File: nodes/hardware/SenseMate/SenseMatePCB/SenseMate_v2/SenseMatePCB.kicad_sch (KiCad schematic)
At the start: 15 parts, among them J1 Conn_01x04, M1 Motor_DC, Q1 2SC1815, Q2 2SC1815, SW5 SW_DPDT_x2, U1 XIAO-nRF52840-Plus-SMD, U2 RFM95W-868S2

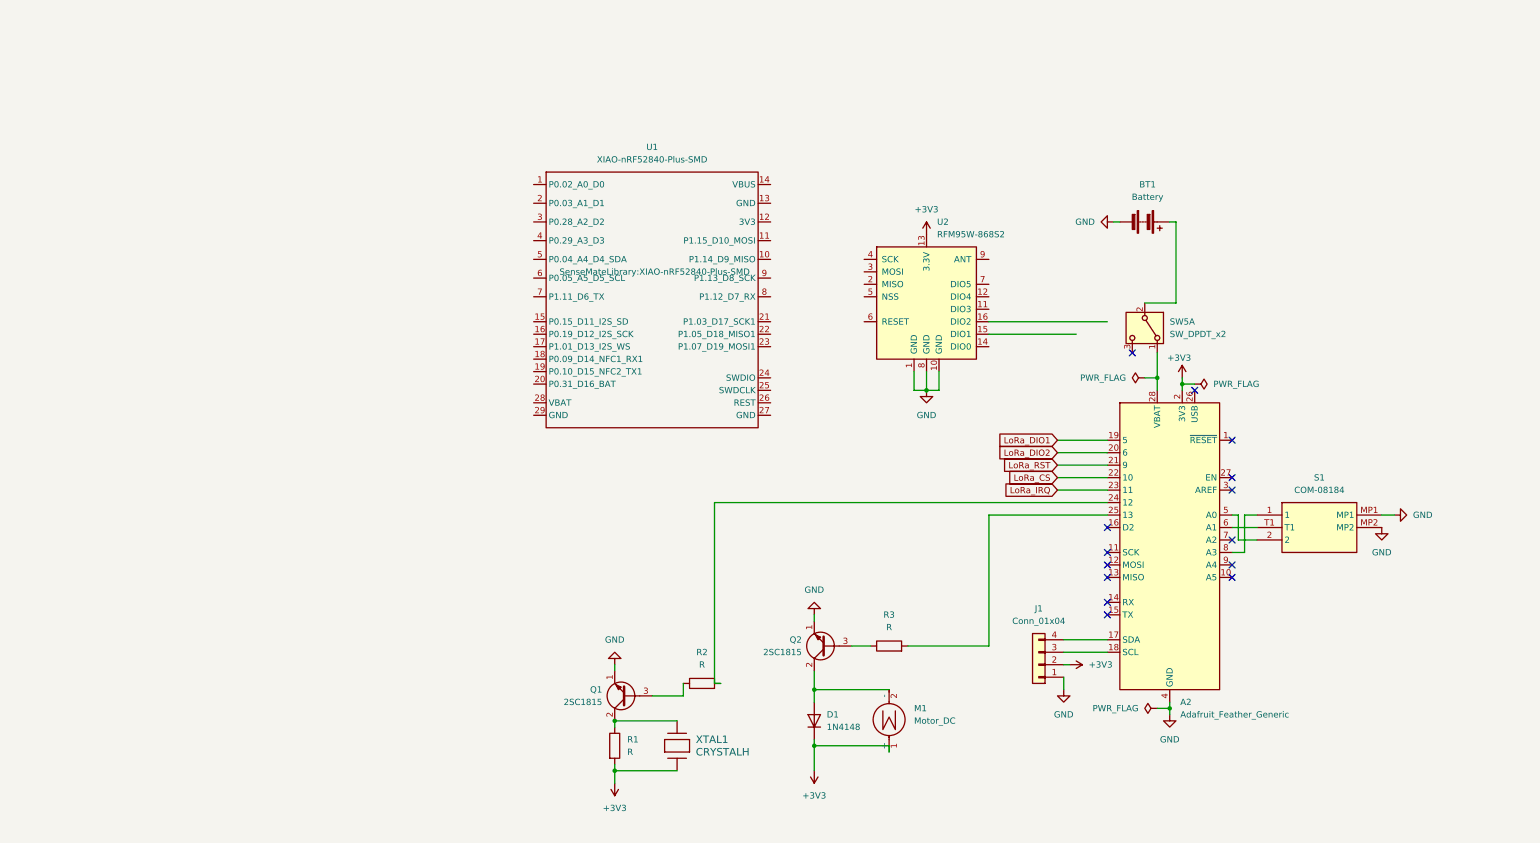
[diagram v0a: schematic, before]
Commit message: Aktualisierung der Verbindungen und Kommentare für offene Verbindungen.
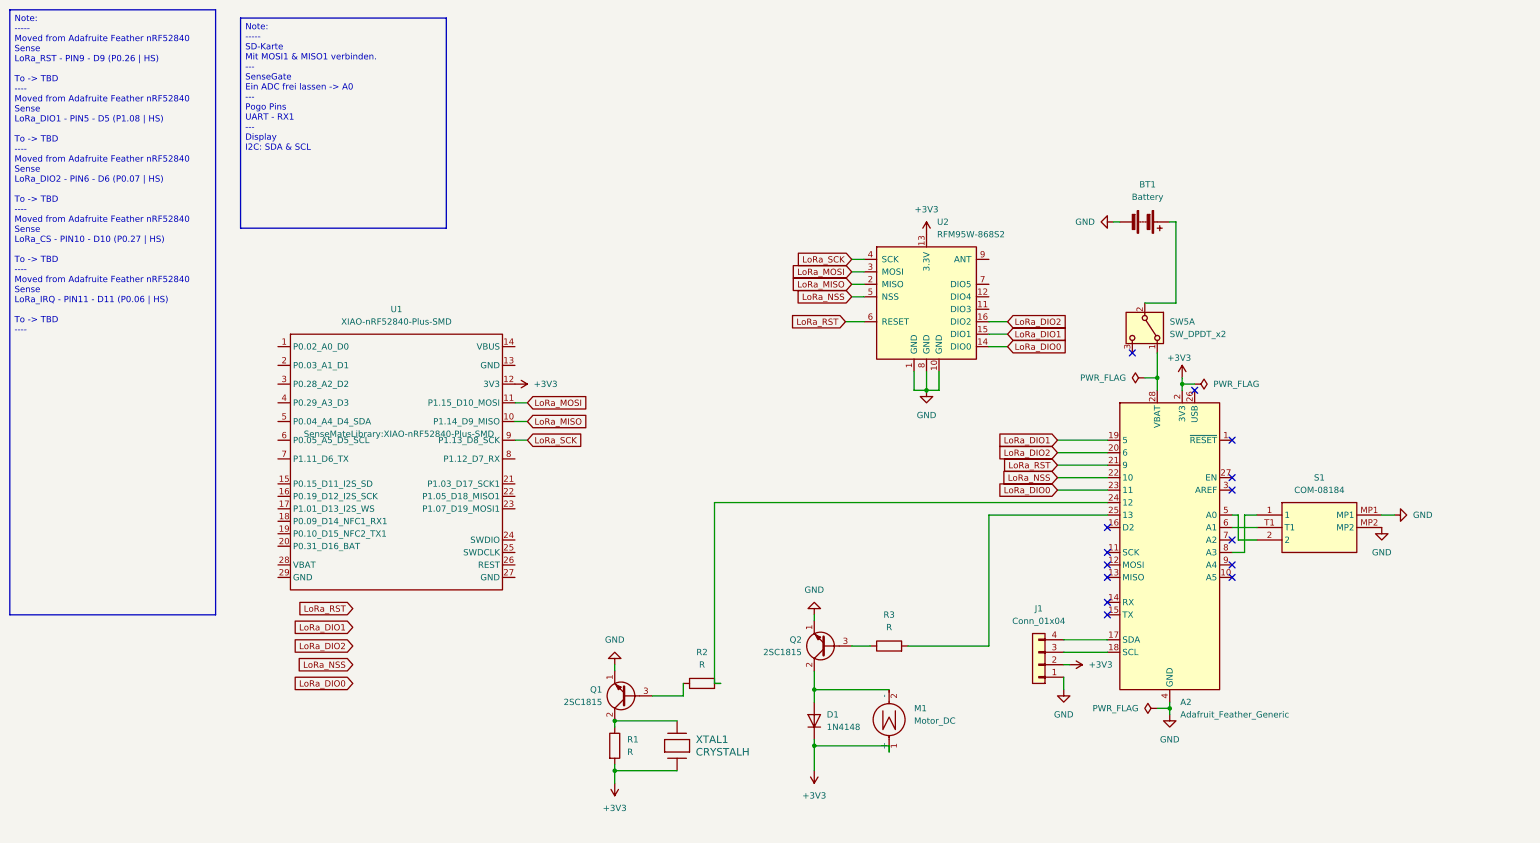
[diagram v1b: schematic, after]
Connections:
- net LoRa_CS is gone; now on net LoRa_NSS: A2.22 (10)
- net LoRa_IRQ is gone; now on net LoRa_DIO0: A2.23 (11)
- net +3V3: now also U1.12 (3V3)
- net LoRa_DIO1: now also U2.15 (DIO1)
- net LoRa_DIO2: now also U2.16 (DIO2)
- net LoRa_RST: now also U2.6 (RESET)
- net LoRa_DIO0: now reaches U2.14 (DIO0)
- net LoRa_MISO: now reaches U2.2 (MISO)
- net LoRa_MISO: now also U1.10 (P1.14_D9_MISO)
- net LoRa_MOSI: now reaches U2.3 (MOSI)
- net LoRa_MOSI: now also U1.11 (P1.15_D10_MOSI)
- net LoRa_SCK: now reaches U2.4 (SCK)
- net LoRa_SCK: now also U1.9 (P1.13_D8_SCK)
- net LoRa_NSS: now reaches U2.5 (NSS)
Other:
- moved on the sheet: U1

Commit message: 26-finished marking used pins
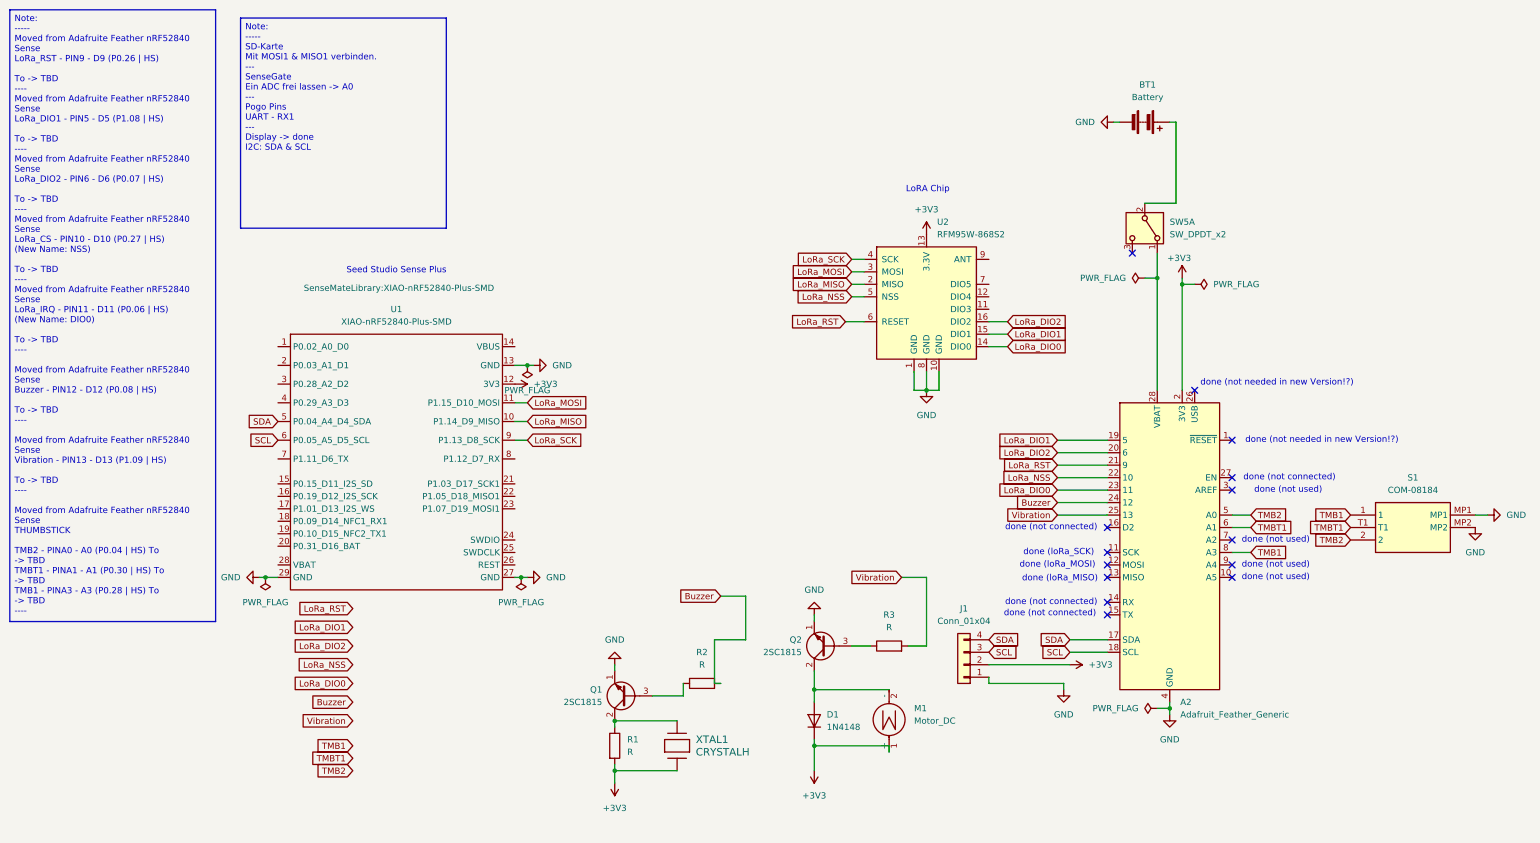
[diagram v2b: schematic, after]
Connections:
- net GND: now also U1.13 (GND), U1.27 (GND), U1.29 (GND)
- net SDA: now reaches A2.17 (SDA), J1.4 (Pin_4)
- net SDA: now also U1.5 (P0.04_A4_D4_SDA)
- net SCL: now reaches A2.18 (SCL), J1.3 (Pin_3)
- net SCL: now also U1.6 (P0.05_A5_D5_SCL)
- net Buzzer: now reaches A2.24 (12), R2.2
- net Vibration: now reaches A2.25 (13), R3.2
- net TMB2: now reaches A2.5 (A0), S1.2
- net TMBT1: now reaches A2.6 (A1), S1.T1
- net TMB1: now reaches A2.8 (A3), S1.1
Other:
- note added: "LoRA Chip"
- note added: "Seed Studio Sense Plus"
- note added: "done (loRa_MISO)"
- note added: "done (loRa_MOSI)"
- note added: "done (loRa_SCK)"
- note added: "done (not connected)"
- note added: "done (not needed in new Version!?)"
- note added: "done (not used)"
- moved on the sheet: BT1, J1, S1, SW5A

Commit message: 26-finished all connections from feather carried over
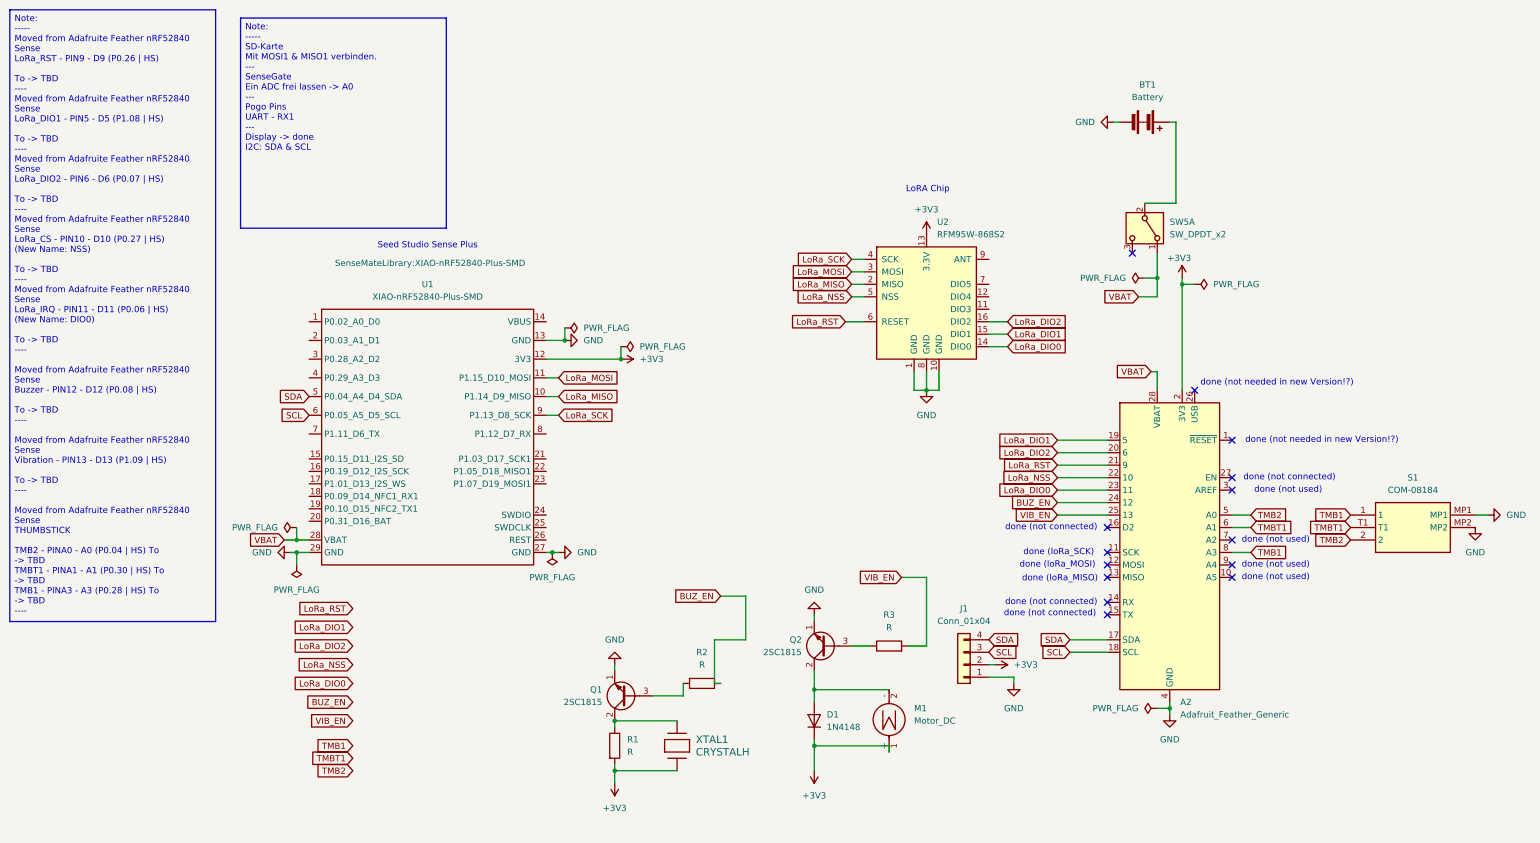
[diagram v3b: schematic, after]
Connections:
- net VBAT: now reaches A2.28 (VBAT), SW5.1 (A)
- net VBAT: now also U1.28 (VBAT)
- net Buzzer renamed BUZ_EN
- net Vibration renamed VIB_EN
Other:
- moved on the sheet: U1

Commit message: 26-Finalisierung der Verbindunen zwischen den Geräten und Aufräumen des Schemas
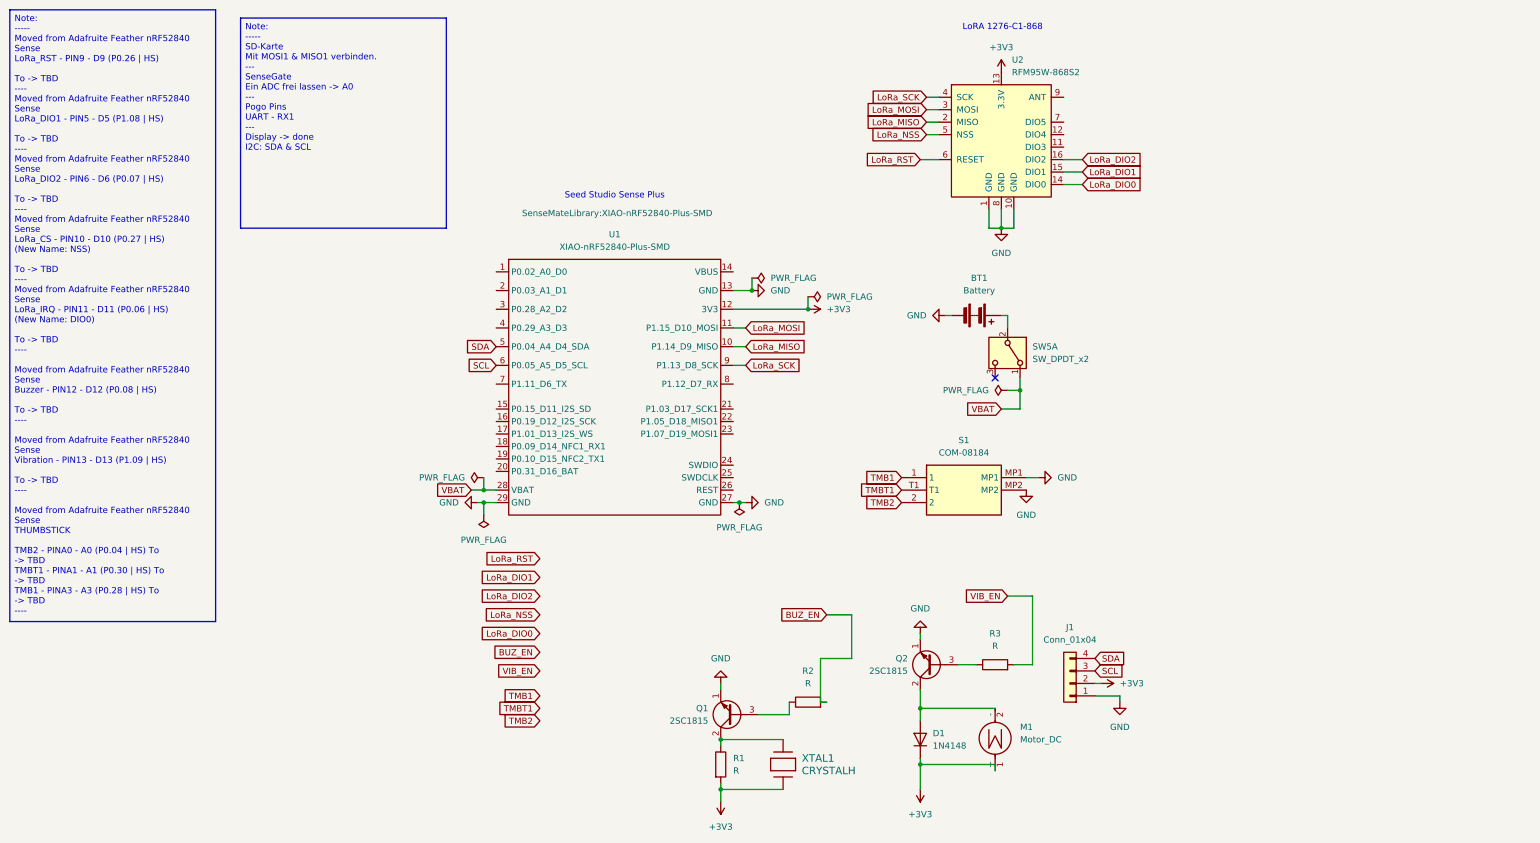
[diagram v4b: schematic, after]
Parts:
- removed A2: Adafruit_Feather_Generic, SenseMateLibrary:Adafruit_Feather_Sense, symbol SenseMateLibrary:Adafruit_Feather_Generic
- SW5: footprint SenseMate_Pwr_Button_:OS102011MA1QN1 -> SenseMateLibrary:OS102011MA1QN1
- XTAL1: footprint XTAL_PS1240P02BT_TDK -> SenseMateLibrary:PS1240P02BT
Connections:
- no-connect marks 14 -> 1
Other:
- note added: "LoRA 1276-C1-868"
- note removed: "LoRA Chip"
- note removed: "done (loRa_MISO)"
- note removed: "done (loRa_MOSI)"
- note removed: "done (loRa_SCK)"
- note removed: "done (not connected)"
- note removed: "done (not needed in new Version!?)"
- note removed: "done (not used)"
- moved on the sheet: BT1, D1, J1, M1, Q1, Q2, R1, R2, R3, S1, SW5A, U1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

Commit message: fehlende 3D symboly für SeedStudio und LoraChip hinzugefügt, Netzte Verbunden, Kommentare ergänzt
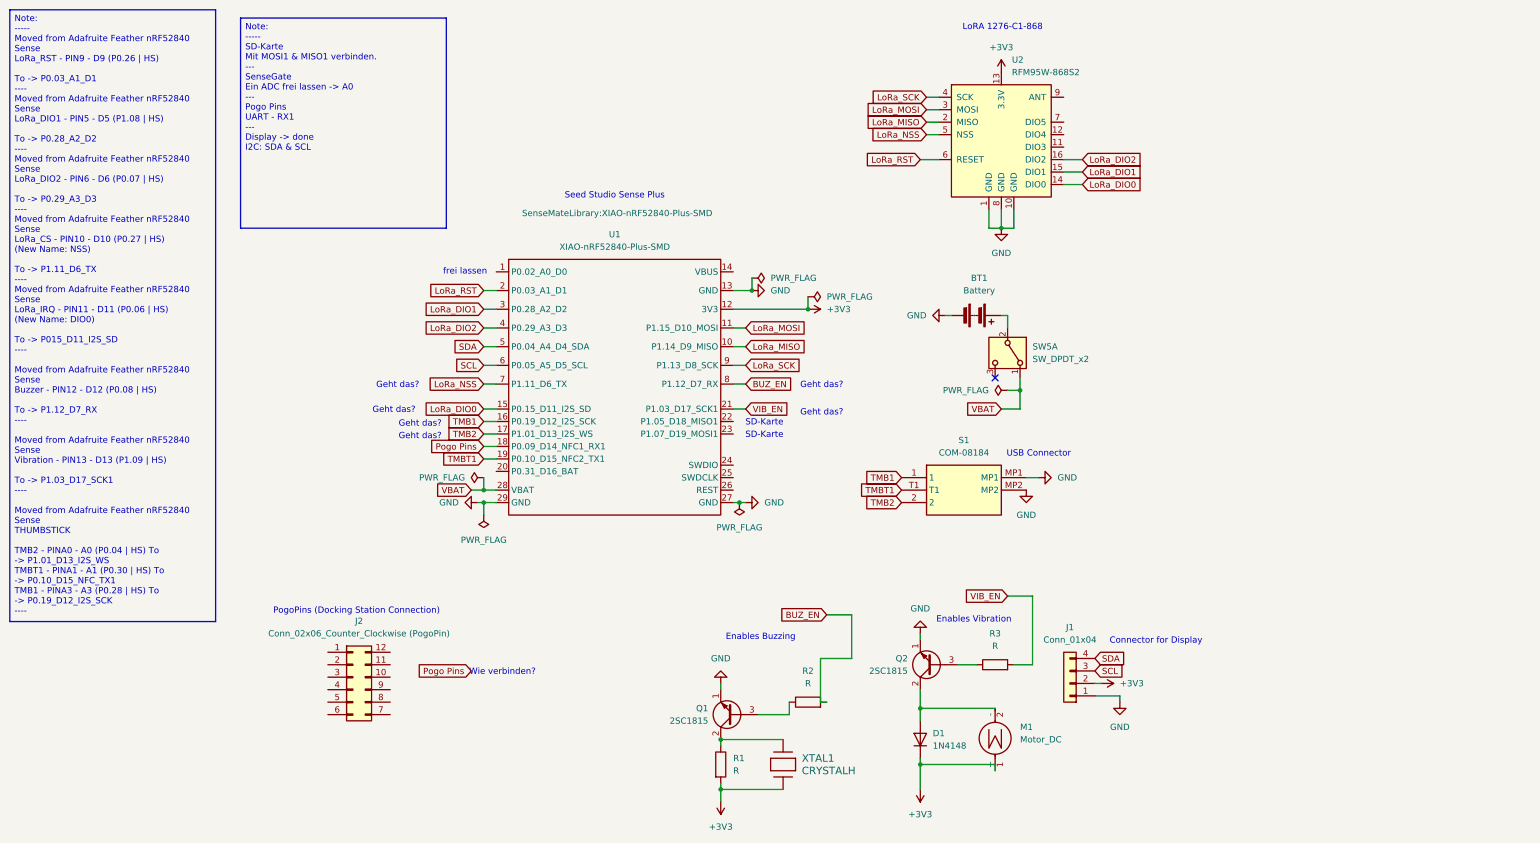
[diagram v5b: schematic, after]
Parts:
- added J2: Conn_02x06_Counter_Clockwise (PogoPin), Connector_PinHeader_1.27mm:PinHeader_1x06_P1.27mm_Vertical, symbol Connector_Generic:Conn_02x06_Counter_Clockwise
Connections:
- net BUZ_EN: now also U1.8 (P1.12_D7_RX)
- net LoRa_DIO0: now also U1.15 (P0.15_D11_I2S_SD)
- net LoRa_DIO1: now also U1.3 (P0.28_A2_D2)
- net LoRa_DIO2: now also U1.4 (P0.29_A3_D3)
- net LoRa_NSS: now also U1.7 (P1.11_D6_TX)
- net LoRa_RST: now also U1.2 (P0.03_A1_D1)
- net TMB1: now also U1.16 (P0.19_D12_I2S_SCK)
- net TMB2: now also U1.17 (P1.01_D13_I2S_WS)
- net TMBT1: now also U1.19 (P0.10_D15_NFC2_TX1)
- net VIB_EN: now also U1.21 (P1.03_D17_SCK1)
- net Pogo Pins: now reaches U1.18 (P0.09_D14_NFC1_RX1)
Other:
- note added: "Connector for Display"
- note added: "Enables Buzzing"
- note added: "Enables Vibration"
- note added: "Geht das?"
- note added: "PogoPins (Docking Station Connection)"
- note added: "SD-Karte"
- note added: "USB Connector"
- note added: "Wie verbinden?"
- note added: "frei lassen"
